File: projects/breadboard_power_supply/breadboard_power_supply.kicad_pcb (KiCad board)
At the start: 2 copper layers, 10 parts, among them J1 Barrel_Jack_Switch, U1 LM7805_TO220, U2 LM317_TO-220

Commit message: Best practices for libraries in breadboard_power_supply project
- move libraries/ folder inside main project folder
- make paths references relative using ${KIPRJMOD} variable
- modify .gitignore to commit fp-lib-table and sym-lib-table
- update links to MH_Slider_Switch symbol and footprint in KiCAD files
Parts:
- S1: footprint Slide_Switch:SW_OS102011MS2QN1 -> MH_Slide_Switch:SW_OS102011MS2QN1
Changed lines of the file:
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@@
 		)
 	)
-	(footprint "Slide_Switch:SW_OS102011MS2QN1"
+	(footprint "MH_Slide_Switch:SW_OS102011MS2QN1"
 		(layer "F.Cu")
 		(at 101 64)

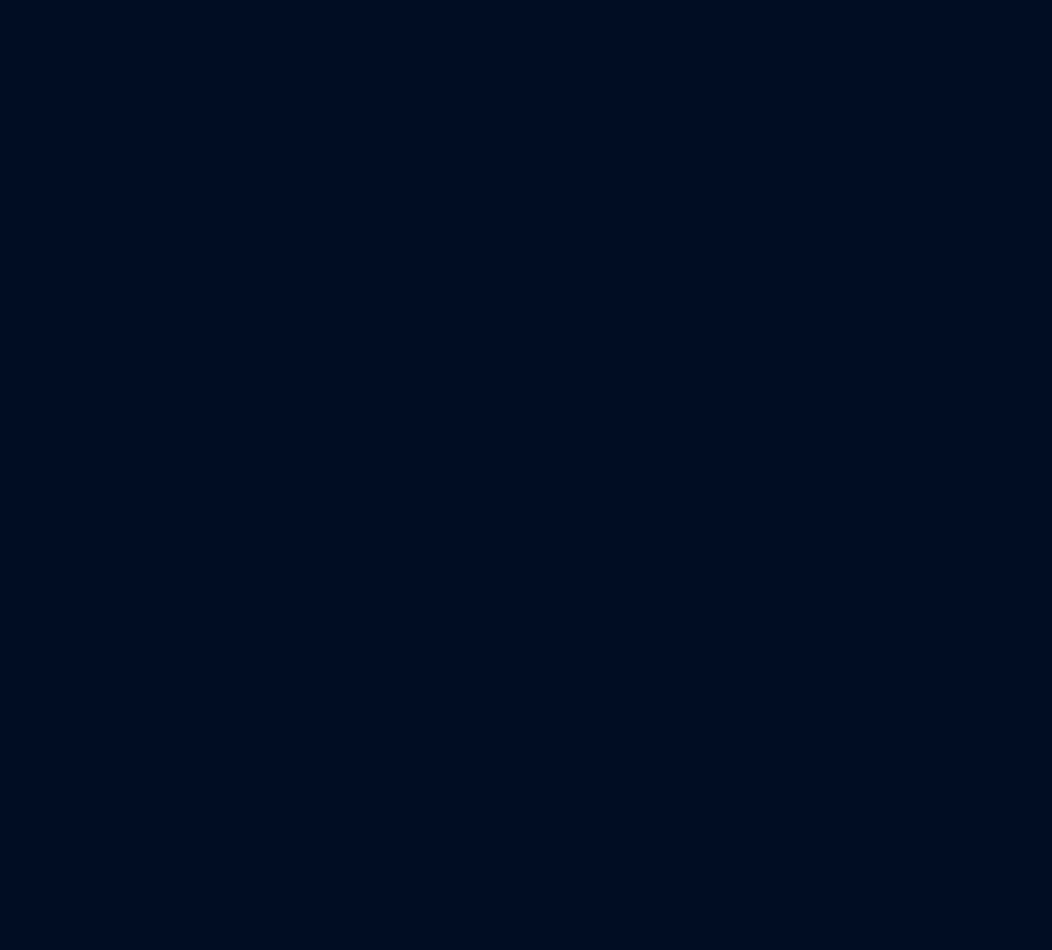
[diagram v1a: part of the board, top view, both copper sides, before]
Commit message: Complete associations, start wiring
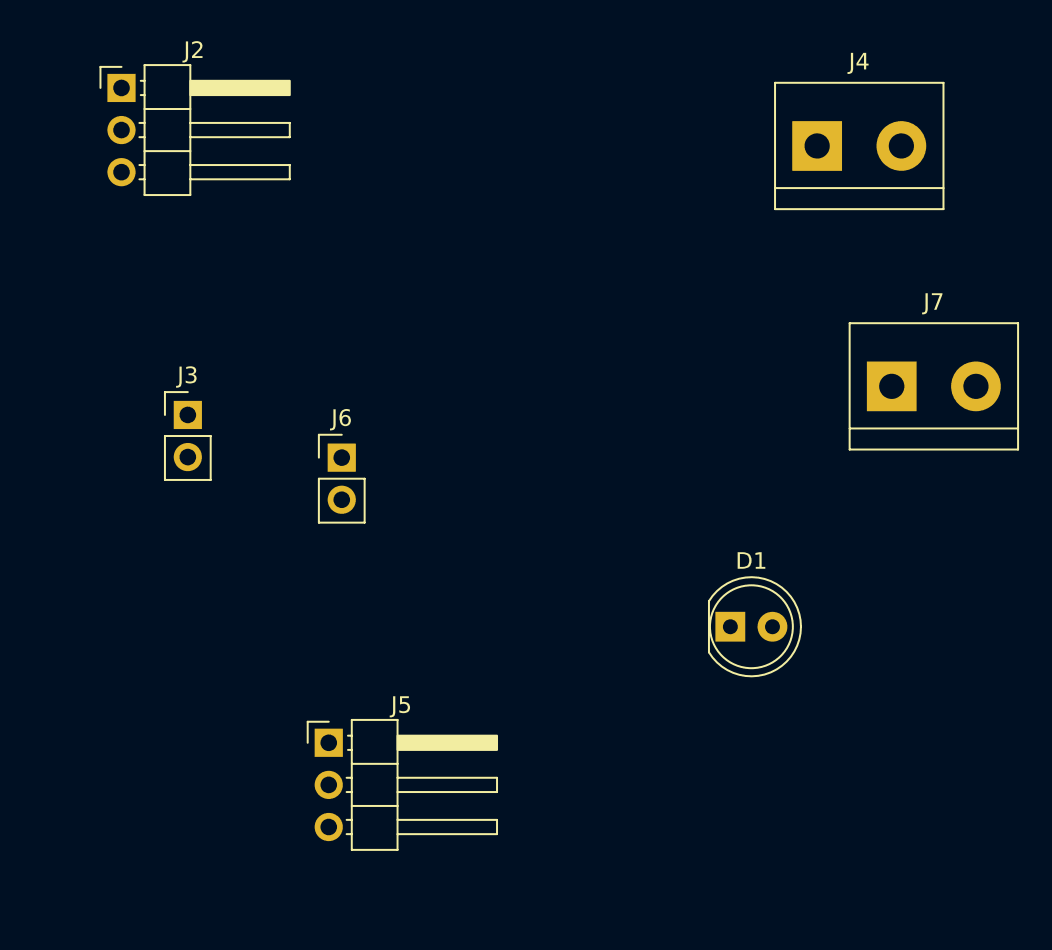
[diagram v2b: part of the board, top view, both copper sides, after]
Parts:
- added D1: LED, LED_THT:LED_D5.0mm, F.Cu at (234.2, 77.0)
- added J2: Conn_01x03_Pin, Connector_PinHeader_2.54mm:PinHeader_1x03_P2.54mm_Horizontal, F.Cu at (197.5, 44.5)
- added J3: Conn_01x02_Pin, Connector_PinHeader_2.54mm:PinHeader_1x02_P2.54mm_Vertical, F.Cu at (201.5, 64.2)
- added J4: Screw_Terminal_01x02, TerminalBlock:TerminalBlock_bornier-2_P5.08mm, F.Cu at (239.5, 48.0)
- added J5: Conn_01x03_Pin, Connector_PinHeader_2.54mm:PinHeader_1x03_P2.54mm_Horizontal, F.Cu at (210.0, 84.0)
- added J6: Conn_01x02_Pin, Connector_PinHeader_2.54mm:PinHeader_1x02_P2.54mm_Vertical, F.Cu at (210.8, 66.8)
- added J7: Screw_Terminal_01x02, TerminalBlock:TerminalBlock_bornier-2_P5.08mm, F.Cu at (244.0, 62.5)

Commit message: Name Nets
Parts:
- renumbered J7 to J6, J6 to J7, U2 to U1, U1 to U2
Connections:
- C1 pad 1: unconnected-(C1-Pad1) -> GND
- C1 pad 2: unconnected-(C1-Pad2) -> /12V
- C2 pad 1: unconnected-(C2-Pad1) -> GND
- C2 pad 2: unconnected-(C2-Pad2) -> /5V
- C3 pad 1: unconnected-(C3-Pad1) -> GND
- C3 pad 2: unconnected-(C3-Pad2) -> /3.3V
- D1 pad 1: unconnected-(D1-K-Pad1) -> GND
- D1 pad 2: unconnected-(D1-A-Pad2) -> Net-(D1-A)
- J1 pad 1: unconnected-(J1-Pad1) -> /PWR_input
- J1 pad 2: unconnected-(J1-Pad2) -> GND
- J1 pad 3: unconnected-(J1-Pad3) -> GND
- J2 pad 1: unconnected-(J2-Pin_1-Pad1) -> /3.3V
- J2 pad 2: unconnected-(J2-Pin_2-Pad2) -> /PWR_output
- J2 pad 3: unconnected-(J2-Pin_3-Pad3) -> /5V
- J3 pad 1: unconnected-(J3-Pin_1-Pad1) -> GND
- J3 pad 2: unconnected-(J3-Pin_2-Pad2) -> /PWR_output
- J4 pad 1: unconnected-(J4-Pin_1-Pad1) -> GND
- J4 pad 2: unconnected-(J4-Pin_2-Pad2) -> /PWR_output
- J5 pad 1: unconnected-(J5-Pin_1-Pad1) -> /3.3V
- J5 pad 2: unconnected-(J5-Pin_2-Pad2) -> /PWR_output
- J5 pad 3: unconnected-(J5-Pin_3-Pad3) -> /5V
- J6 pad 1: unconnected-(J7-Pin_1-Pad1) -> GND
- J6 pad 2: unconnected-(J7-Pin_2-Pad2) -> /PWR_output
- J7 pad 1: unconnected-(J6-Pin_1-Pad1) -> GND
- J7 pad 2: unconnected-(J6-Pin_2-Pad2) -> /PWR_output
- R1 pad 1: unconnected-(R1-Pad1) -> /12V
- R1 pad 2: unconnected-(R1-Pad2) -> Net-(D1-A)
- R2 pad 1: unconnected-(R2-Pad1) -> Net-(U1-ADJ)
- R2 pad 2: unconnected-(R2-Pad2) -> /3.3V
- R3 pad 1: unconnected-(R3-Pad1) -> GND
- R3 pad 2: unconnected-(R3-Pad2) -> Net-(U1-ADJ)
- S1 pad 1: unconnected-(S1-Pad1) -> /12V
- S1 pad 2: unconnected-(S1-Pad2) -> /PWR_input
- U1 pad 1: unconnected-(U2-ADJ-Pad1) -> Net-(U1-ADJ)
- U1 pad 2: unconnected-(U2-VO-Pad2) -> /3.3V
- U1 pad 3: unconnected-(U2-VI-Pad3) -> /12V
- U2 pad 1: unconnected-(U1-VI-Pad1) -> /12V
- U2 pad 2: unconnected-(U1-GND-Pad2) -> GND
- U2 pad 3: unconnected-(U1-VO-Pad3) -> /5V
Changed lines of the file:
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@@
 	)
 	(net 0 "")
-	(net 1 "unconnected-(C1-Pad2)")
-	(net 2 "unconnected-(C1-Pad1)")
-	(net 3 "unconnected-(C2-Pad2)")
-	(net 4 "unconnected-(C2-Pad1)")
-	(net 5 "unconnected-(C3-Pad1)")
-	(net 6 "unconnected-(C3-Pad2)")
-	(net 7 "unconnected-(J1-Pad1)")
-	(net 8 "unconnected-(J1-Pad2)")
-	(net 9 "unconnected-(J1-Pad3)")
-	(net 10 "unconnected-(R1-Pad2)")
-	(net 11 "unconnected-(R1-Pad1)")
-	(net 12 "unconnected-(R2-Pad1)")
-	(net 13 "unconnected-(R2-Pad2)")
-	(net 14 "unconnected-(R3-Pad1)")
-	(net 15 "unconnected-(R3-Pad2)")
-	(net 16 "unconnected-(U1-GND-Pad2)")
-	(net 17 "unconnected-(U1-VI-Pad1)")
-	(net 18 "unconnected-(U1-VO-Pad3)")
-	(net 19 "unconnected-(U2-VO-Pad2)")
-	(net 20 "unconnected-(U2-ADJ-Pad1)")
-	(net 21 "unconnected-(U2-VI-Pad3)")
-	(net 22 "unconnected-(S1-Pad3)")
-	(net 23 "unconnected-(S1-Pad1)")
-	(net 24 "unconnected-(S1-Pad2)")
-	(net 25 "unconnected-(D1-K-Pad1)")
-	(net 26 "unconnected-(D1-A-Pad2)")
-	(net 27 "unconnected-(J2-Pin_1-Pad1)")
-	(net 28 "unconnected-(J2-Pin_3-Pad3)")
-	(net 29 "unconnected-(J2-Pin_2-Pad2)")
-	(net 30 "unconnected-(J3-Pin_1-Pad1)")
-	(net 31 "unconnected-(J3-Pin_2-Pad2)")
-	(net 32 "unconnected-(J4-Pin_1-Pad1)")
-	(net 33 "unconnected-(J4-Pin_2-Pad2)")
-	(net 34 "unconnected-(J5-Pin_3-Pad3)")
-	(net 35 "unconnected-(J5-Pin_1-Pad1)")
-	(net 36 "unconnected-(J5-Pin_2-Pad2)")
-	(net 37 "unconnected-(J6-Pin_1-Pad1)")
-	(net 38 "unconnected-(J6-Pin_2-Pad2)")
-	(net 39 "unconnected-(J7-Pin_1-Pad1)")
-	(net 40 "unconnected-(J7-Pin_2-Pad2)")
+	(net 1 "/12V")
+	(net 2 "GND")
+	(net 3 "/5V")
+	(net 4 "/3.3V")
+	(net 5 "Net-(D1-A)")
+	(net 6 "/PWR_input")
+	(net 7 "/PWR_output")
+	(net 8 "Net-(U1-ADJ)")
+	(net 9 "unconnected-(S1-Pad3)")
 	(footprint "Connector_PinHeader_2.54mm:PinHeader_1x02_P2.54mm_Vertical"
 		(layer "F.Cu")
@@
 			(layers "*.Cu" "*.Mask")
 			(remove_unused_layers no)
-			(net 30 "unconnected-(J3-Pin_1-Pad1)")
+			(net 2 "GND")
 			(pinfunction "Pin_1")
 			(pintype "passive")
@@
 			(layers "*.Cu" "*.Mask")
 			(remove_unused_layers no)
-			(net 31 "unconnected-(J3-Pin_2-Pad2)")
+			(net 7 "/PWR_output")
 			(pinfunction "Pin_2")
 			(pintype "passive")
@@
 			(layers "*.Cu" "*.Mask")
 			(remove_unused_layers no)
-			(net 25 "unconnected-(D1-K-Pad1)")
+			(net 2 "GND")
 			(pinfunction "K")
 			(pintype "passive")
@@
 			(layers "*.Cu" "*.Mask")
 			(remove_unused_layers no)
-			(net 26 "unconnected-(D1-A-Pad2)")
+			(net 5 "Net-(D1-A)")
 			(pinfunction "A")
 			(pintype "passive")
@@
 			(layers "*.Cu" "*.Mask")
 			(remove_unused_layers no)
-			(net 27 "unconnected-(J2-Pin_1-Pad1)")
+			(net 4 "/3.3V")
 			(pinfunction "Pin_1")
 			(pintype "passive")
@@
 			(layers "*.Cu" "*.Mask")
 			(remove_unused_layers no)
-			(net 29 "unconnected-(J2-Pin_2-Pad2)")
+			(net 7 "/PWR_output")
 			(pinfunction "Pin_2")
 			(pintype "passive")
@@
 			(layers "*.Cu" "*.Mask")
 			(remove_unused_layers no)
-			(net 28 "unconnected-(J2-Pin_3-Pad3)")
+			(net 3 "/5V")
 			(pinfunction "Pin_3")
 			(pintype "passive")
@@
 			(layers "F.Cu" "F.Mask" "F.Paste")
 			(roundrect_rratio 0.25)
-			(net 11 "unconnected-(R1-Pad1)")
+			(net 1 "/12V")
 			(pintype "passive")
 		)
@@
 			(layers "F.Cu" "F.Mask" "F.Paste")
 			(roundrect_rratio 0.25)
-			(net 10 "unconnected-(R1-Pad2)")
+			(net 5 "Net-(D1-A)")
 			(pintype "passive")
 		)
@@
 		(descr "TO-220-3, Vertical, RM 2.54mm, see https://www.vishay.com/docs/66542/to-220-1.pdf, generated with kicad-footprint-generator TO_SOT_THT_generate.py")
 		(tags "TO-220-3 Vertical RM 2.54mm")
-		(property "Reference" "U1"
+		(property "Reference" "U2"
 			(at 2.54 -4.1 0)
 			(layer "F.SilkS")
@@
 			(layers "*.Cu" "*.Mask")
 			(remove_unused_layers no)
-			(net 17 "unconnected-(U1-VI-Pad1)")
+			(net 1 "/12V")
 			(pinfunction "VI")
 			(pintype "power_in")
@@
 			(layers "*.Cu" "*.Mask")
 			(remove_unused_layers no)
-			(net 16 "unconnected-(U1-GND-Pad2)")
+			(net 2 "GND")
 			(pinfunction "GND")
 			(pintype "power_in")
@@
 			(layers "*.Cu" "*.Mask")
 			(remove_unused_layers no)
-			(net 18 "unconnected-(U1-VO-Pad3)")
+			(net 3 "/5V")
 			(pinfunction "VO")
 			(pintype "power_out")
@@
 			(layers "F.Cu" "F.Mask" "F.Paste")
 			(roundrect_rratio 0.25)
-			(net 4 "unconnected-(C2-Pad1)")
+			(net 2 "GND")
 			(pintype "passive")
 		)
@@
 			(layers "F.Cu" "F.Mask" "F.Paste")
 			(roundrect_rratio 0.25)
-			(net 3 "unconnected-(C2-Pad2)")
+			(net 3 "/5V")
 			(pintype "passive")
 		)
@@
 			(layers "F.Cu" "F.Mask" "F.Paste")
 			(roundrect_rratio 0.25)
-			(net 14 "unconnected-(R3-Pad1)")
+			(net 2 "GND")
 			(pintype "passive")
 		)
@@
 			(layers "F.Cu" "F.Mask" "F.Paste")
 			(roundrect_rratio 0.25)
-			(net 15 "unconnected-(R3-Pad2)")
+			(net 8 "Net-(U1-ADJ)")
 			(pintype "passive")
 		)
@@
 			(layers "*.Cu" "*.Mask")
 			(remove_unused_layers no)
-			(net 23 "unconnected-(S1-Pad1)")
+			(net 1 "/12V")
 			(pinfunction "1")
 			(pintype "passive")
@@
 			(layers "*.Cu" "*.Mask")
 			(remove_unused_layers no)
-			(net 24 "unconnected-(S1-Pad2)")
+			(net 6 "/PWR_input")
 			(pinfunction "2")
 			(pintype "passive")
@@
 			(layers "*.Cu" "*.Mask")
 			(remove_unused_layers no)
-			(net 22 "unconnected-(S1-Pad3)")
+			(net 9 "unconnected-(S1-Pad3)")
 			(pinfunction "3")
-			(pintype "passive")
+			(pintype "passive+no_connect")
 			(solder_mask_margin 0.102)
 		)
@@
 		(descr "simple 2-pin terminal block, pitch 5.08mm, revamped version of bornier2")
 		(tags "terminal block bornier2")
-		(property "Reference" "J7"
+		(property "Reference" "J6"
 			(at 2.54 -5.08 0)
 			(layer "F.SilkS")
@@
 			(layers "*.Cu" "*.Mask")
 			(remove_unused_layers no)
-			(net 39 "unconnected-(J7-Pin_1-Pad1)")
+			(net 2 "GND")
 			(pinfunction "Pin_1")
 			(pintype "passive")
@@
 			(layers "*.Cu" "*.Mask")
 			(remove_unused_layers no)
-			(net 40 "unconnected-(J7-Pin_2-Pad2)")
+			(net 7 "/PWR_output")
 			(pinfunction "Pin_2")
 			(pintype "passive")
@@
 		(descr "Through hole straight pin header, 1x02, 2.54mm pitch, single row")
 		(tags "Through hole pin header THT 1x02 2.54mm single row")
-		(property "Reference" "J6"
+		(property "Reference" "J7"
 			(at 0 -2.38 0)
 			(layer "F.SilkS")
@@
 			(layers "*.Cu" "*.Mask")
 			(remove_unused_layers no)
-			(net 37 "unconnected-(J6-Pin_1-Pad1)")
+			(net 2 "GND")
 			(pinfunction "Pin_1")
 			(pintype "passive")
@@
 			(layers "*.Cu" "*.Mask")
 			(remove_unused_layers no)
-			(net 38 "unconnected-(J6-Pin_2-Pad2)")
+			(net 7 "/PWR_output")
 			(pinfunction "Pin_2")
 			(pintype "passive")
@@
 			(layers "*.Cu" "*.Mask")
 			(remove_unused_layers no)
-			(net 7 "unconnected-(J1-Pad1)")
+			(net 6 "/PWR_input")
 			(pintype "passive")
 		)
@@
 			(layers "*.Cu" "*.Mask")
 			(remove_unused_layers no)
-			(net 8 "unconnected-(J1-Pad2)")
+			(net 2 "GND")
 			(pintype "passive")
 		)
@@
 			(layers "*.Cu" "*.Mask")
 			(remove_unused_layers no)
-			(net 9 "unconnected-(J1-Pad3)")
+			(net 2 "GND")
 			(pintype "passive")
 		)
@@
 			(layers "*.Cu" "*.Mask")
 			(remove_unused_layers no)
-			(net 35 "unconnected-(J5-Pin_1-Pad1)")
+			(net 4 "/3.3V")
 			(pinfunction "Pin_1")
 			(pintype "passive")
@@
 			(layers "*.Cu" "*.Mask")
 			(remove_unused_layers no)
-			(net 36 "unconnected-(J5-Pin_2-Pad2)")
+			(net 7 "/PWR_output")
 			(pinfunction "Pin_2")
 			(pintype "passive")
@@
 			(layers "*.Cu" "*.Mask")
 			(remove_unused_layers no)
-			(net 34 "unconnected-(J5-Pin_3-Pad3)")
+			(net 3 "/5V")
 			(pinfunction "Pin_3")
 			(pintype "passive")
@@
 			(layers "*.Cu" "*.Mask")
 			(remove_unused_layers no)
-			(net 32 "unconnected-(J4-Pin_1-Pad1)")
+			(net 2 "GND")
 			(pinfunction "Pin_1")
 			(pintype "passive")
@@
 			(layers "*.Cu" "*.Mask")
 			(remove_unused_layers no)
-			(net 33 "unconnected-(J4-Pin_2-Pad2)")
+			(net 7 "/PWR_output")
 			(pinfunction "Pin_2")
 			(pintype "passive")
@@
 		(descr "TO-220-3, Vertical, RM 2.54mm, see https://www.vishay.com/docs/66542/to-220-1.pdf, generated with kicad-footprint-generator TO_SOT_THT_generate.py")
 		(tags "TO-220-3 Vertical RM 2.54mm")
-		(property "Reference" "U2"
+		(property "Reference" "U1"
 			(at 2.54 -4.1 0)
 			(layer "F.SilkS")
@@
 			(layers "*.Cu" "*.Mask")
 			(remove_unused_layers no)
-			(net 20 "unconnected-(U2-ADJ-Pad1)")
+			(net 8 "Net-(U1-ADJ)")
 			(pinfunction "ADJ")
 			(pintype "input")
@@
 			(layers "*.Cu" "*.Mask")
 			(remove_unused_layers no)
-			(net 19 "unconnected-(U2-VO-Pad2)")
+			(net 4 "/3.3V")
 			(pinfunction "VO")
 			(pintype "power_out")
@@
 			(layers "*.Cu" "*.Mask")
 			(remove_unused_layers no)
-			(net 21 "unconnected-(U2-VI-Pad3)")
+			(net 1 "/12V")
 			(pinfunction "VI")
 			(pintype "power_in")
@@
 			(layers "F.Cu" "F.Mask" "F.Paste")
 			(roundrect_rratio 0.25)
-			(net 5 "unconnected-(C3-Pad1)")
+			(net 2 "GND")
 			(pintype "passive")
 		)
@@
 			(layers "F.Cu" "F.Mask" "F.Paste")
 			(roundrect_rratio 0.25)
-			(net 6 "unconnected-(C3-Pad2)")
+			(net 4 "/3.3V")
 			(pintype "passive")
 		)
@@
 			(layers "F.Cu" "F.Mask" "F.Paste")
 			(roundrect_rratio 0.25)
-			(net 12 "unconnected-(R2-Pad1)")
+			(net 8 "Net-(U1-ADJ)")
 			(pintype "passive")
 		)
@@
 			(layers "F.Cu" "F.Mask" "F.Paste")
 			(roundrect_rratio 0.25)
-			(net 13 "unconnected-(R2-Pad2)")
+			(net 4 "/3.3V")
 			(pintype "passive")
 		)
@@
 			(layers "F.Cu" "F.Mask" "F.Paste")
 			(roundrect_rratio 0.25)
-			(net 2 "unconnected-(C1-Pad1)")
+			(net 2 "GND")
 			(pintype "passive")
 		)
@@
 			(layers "F.Cu" "F.Mask" "F.Paste")
 			(roundrect_rratio 0.25)
-			(net 1 "unconnected-(C1-Pad2)")
+			(net 1 "/12V")
 			(pintype "passive")
 		)

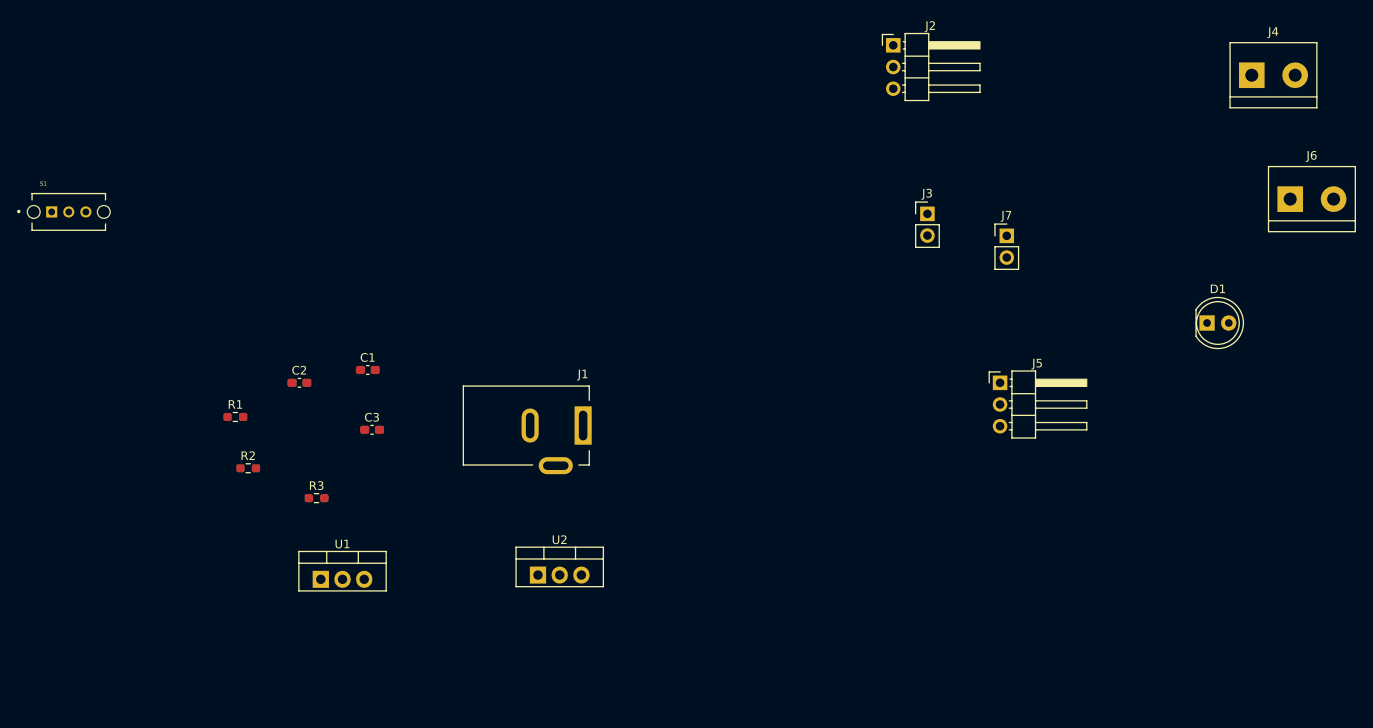
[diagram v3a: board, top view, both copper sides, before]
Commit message: Define net classes, add text and boxes, improve logo
- Add net classes
- Add boxes, text, and graphics to the drawing sheet
- improve color version of logo: blacker lines, round
  junction on the left, clean background
- make b/w version of logo in BMP and then .kicad_mod
  using Image Converter to use as silkscreen logo
- make b/w version in SVG to add as graphic to the
  drawing sheet
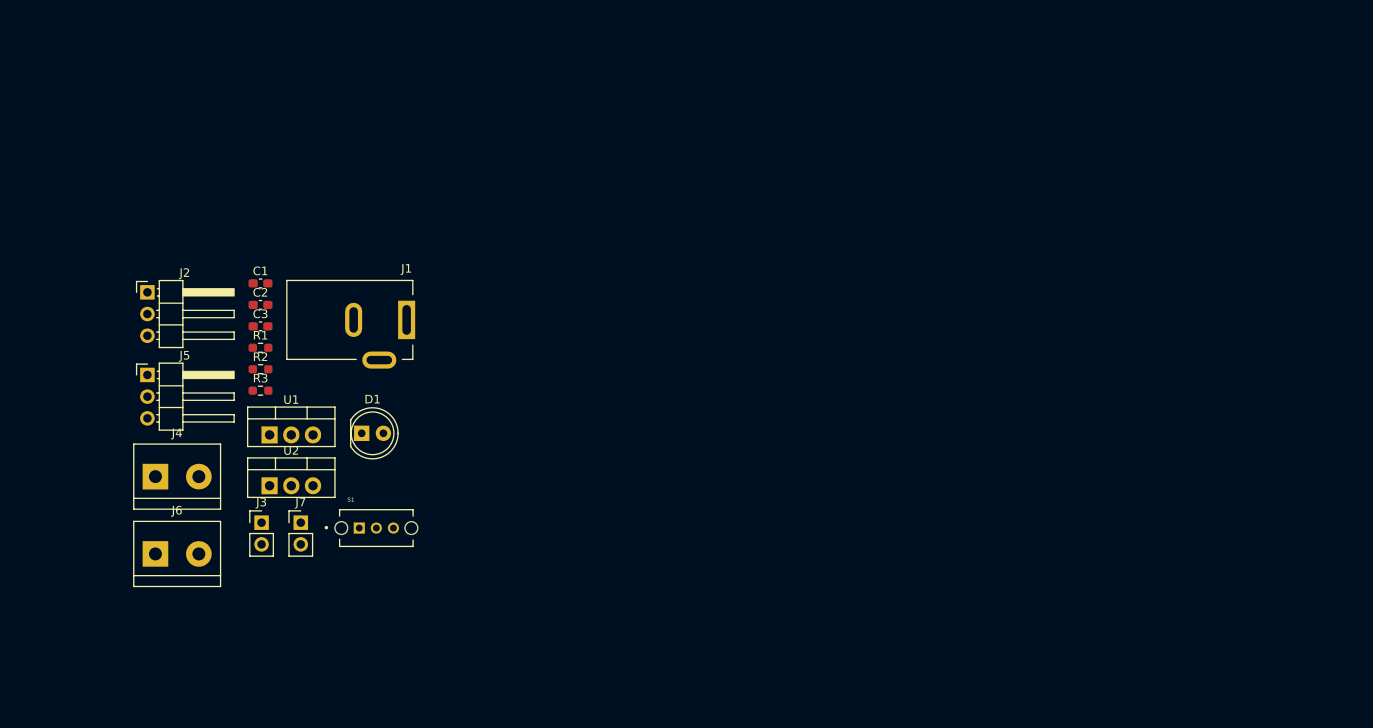
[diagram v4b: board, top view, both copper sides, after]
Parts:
- moved J6 139.2 mm to (111.1, 104.0)
- moved J4 136.6 mm to (111.1, 95.0)
- moved J5 99.8 mm to (110.2, 83.1)
- moved D1 99.8 mm to (135.3, 89.9)
- moved J2 92.0 mm to (110.2, 73.4)
- moved J7 89.2 mm to (128.2, 100.4)
- moved J3 85.9 mm to (123.6, 100.4)
- moved S1 51.6 mm to (137.0, 101.0)
- moved U2 33.1 mm to (124.5, 96.0)
- moved J1 24.1 mm to (140.5, 76.6)
- moved U1 17.9 mm to (124.5, 90.1)
- moved C3 17.8 mm to (123.4, 77.4)
- moved C1 16.1 mm to (123.4, 72.4)
- moved R3 14.2 mm to (123.4, 84.9)
- moved R2 11.7 mm to (123.4, 82.4)
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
